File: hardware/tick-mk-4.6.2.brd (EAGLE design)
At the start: 96 x 53 mm, 38 parts, among them IC1 ATMEGA328P, IC2 DS1307, IC3 L7805, Y1 16MHz, Y2 32.768kHz

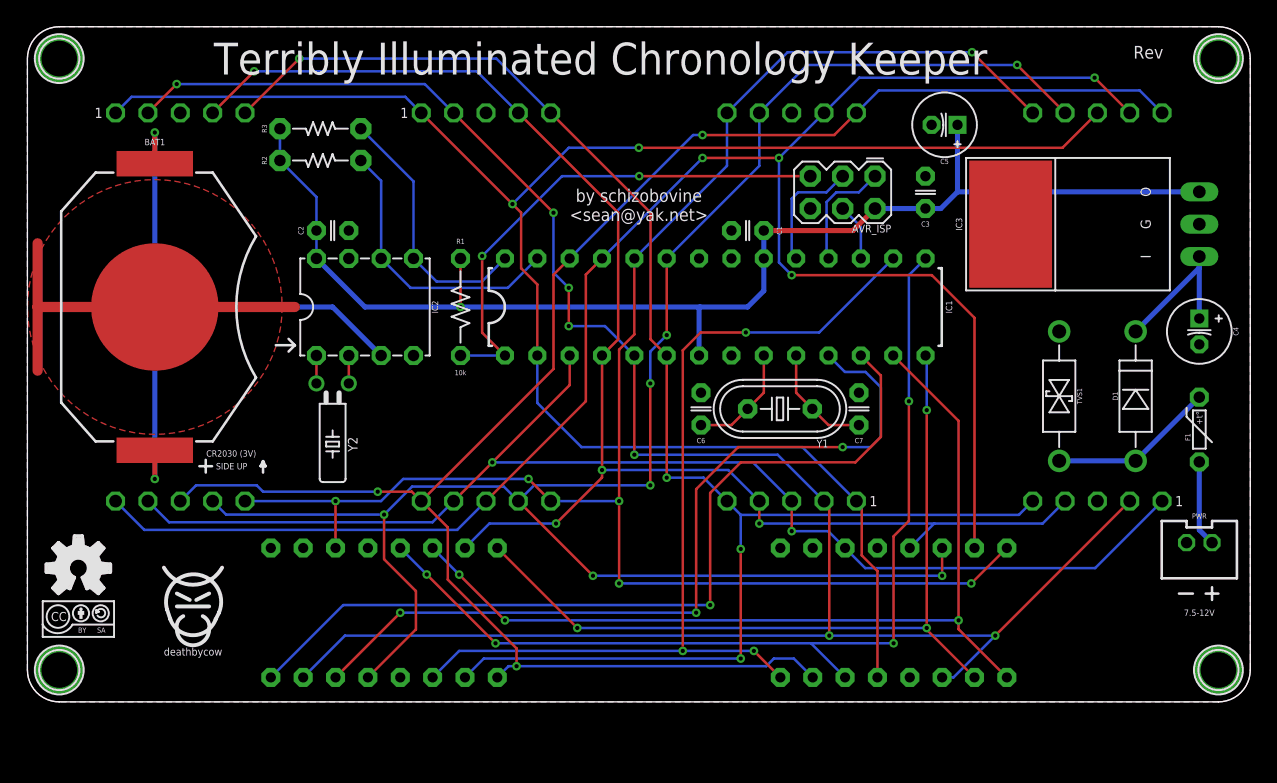
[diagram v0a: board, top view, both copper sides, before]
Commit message: nets complete, now for layout
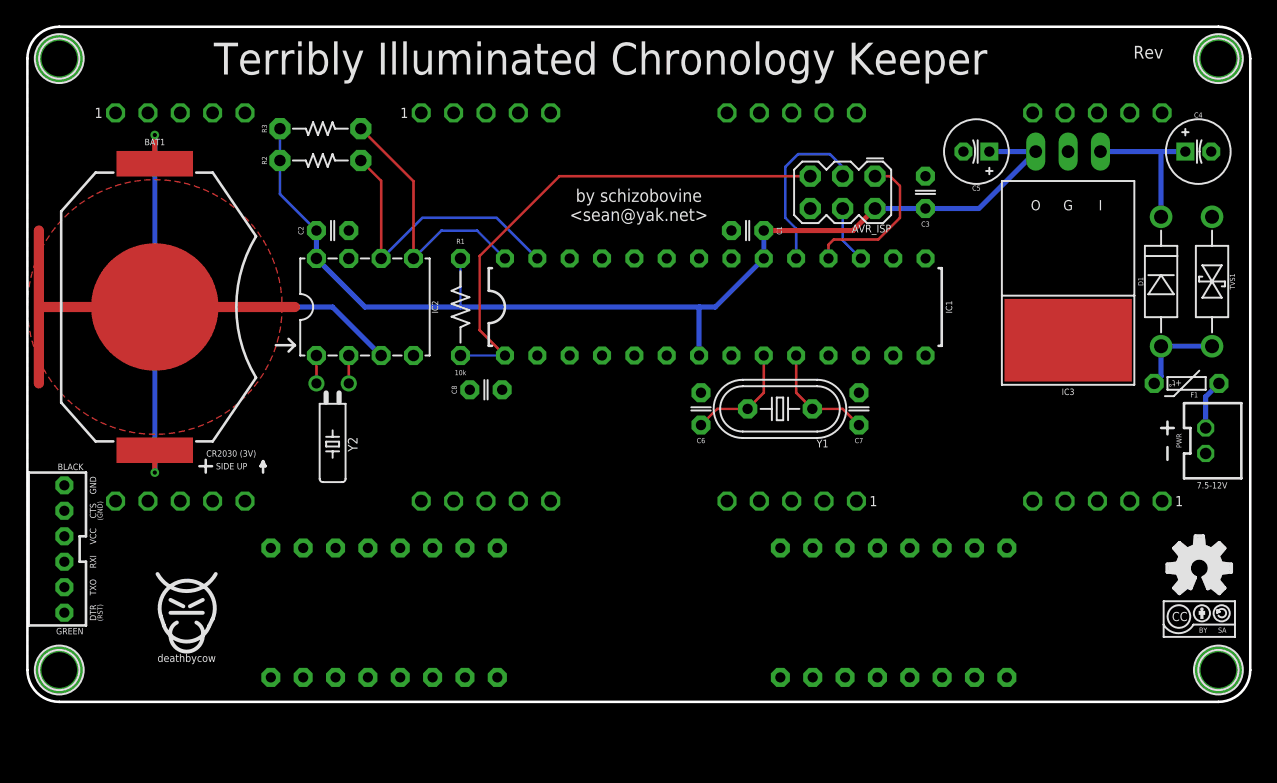
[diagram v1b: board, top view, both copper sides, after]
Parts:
- added C8: 0.1uF, A_butts:C025-024X044
- added JP1: FTDI_CONNJST_PH_VERT_PTH, A_butts:FTDI_CONN_JST_PH_VERT_PTH
- moved U$4 88.0 mm to (92.0, 6.50)
- moved U$5 88.0 mm to (92.0, 10.5)
- moved U$6 88.0 mm to (92.0, 10.5)
- moved U$7 88.0 mm to (92.0, 6.50)
- moved U$3 48.0 mm to (45.0, 19.0)
- moved DISPLAY1 40.0 mm to (68.0, 7.00)
- moved DISPLAY2 40.0 mm to (28.0, 7.00)
- moved TVS1 15.0 mm to (93.0, 33.0)
- moved C4 14.1 mm to (91.9, 43.2), turned to 0 degrees
- moved D1 9.22 mm to (89.0, 33.0)
- moved PWR 8.02 mm to (92.5, 20.5), turned to 270 degrees
- moved IC3 6.76 mm to (81.7, 39.4), turned to 180 degrees
- moved F1 3.76 mm to (91.0, 25.0), turned to 180 degrees
- moved C5 3.26 mm to (74.5, 43.2)
- moved U$2 0.71 mm to (12.5, 7.50)
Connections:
- removed net D0: DIGIT1.8, DIGIT2.1, DIGIT3.1, DIGIT4.1, DISPLAY2.5, IC1.2
- removed net D1: DIGIT1.1, DIGIT2.3, DIGIT3.9, DIGIT4.9, DISPLAY2.11, IC1.3
- new net DTR: C8.1, JP1.DTR
- new net RX: IC1.2, JP1.RXI
- new net TX: IC1.3, JP1.TXO
- net A0: now also DIGIT1.9, DIGIT2.9, DIGIT3.9, DIGIT4.9, DISPLAY1.15, DISPLAY2.11; no longer DIGIT1.7, DIGIT2.7, DIGIT3.7, DIGIT4.7, DISPLAY1.5, DISPLAY2.14
- net A1: now also DIGIT1.10, DIGIT2.10, DIGIT3.10, DIGIT4.10, DISPLAY1.7, DISPLAY2.15; no longer DIGIT1.6, DIGIT2.6, DIGIT3.6, DIGIT4.6, DISPLAY1.11, DISPLAY2.16
- net A2: now also DIGIT1.5, DIGIT2.5, DIGIT3.5, DIGIT4.5, DISPLAY1.14, DISPLAY2.7; no longer DIGIT1.9, DIGIT2.9, DIGIT3.8, DIGIT4.10, DISPLAY2.15
- net A3: no longer DIGIT1.10, DIGIT2.10, DIGIT3.10, DIGIT4.8, DISPLAY1.1, DISPLAY2.7
- net D10: now also DIGIT1.6, DIGIT2.6, DIGIT3.6, DIGIT4.6, DISPLAY2.1; no longer DISPLAY1.3, DISPLAY2.8
- net D11/MOSI: now also DIGIT1.4, DIGIT2.4, DIGIT3.4, DIGIT4.4, DISPLAY2.2
- net D12/MISO: now also DIGIT1.2, DIGIT2.2, DIGIT3.2, DIGIT4.2, DISPLAY2.6
- net D13/SCK: now also DIGIT1.1, DIGIT2.1, DIGIT3.1, DIGIT4.1, DISPLAY1.11, DISPLAY2.8
- net D2: now also DIGIT4.8, DISPLAY1.16, DISPLAY2.14; no longer DIGIT1.4, DIGIT2.4, DIGIT3.4, DIGIT4.4, DISPLAY1.15, DISPLAY2.13
- net D3: now also DIGIT3.8, DISPLAY1.13, DISPLAY2.16; no longer DIGIT1.2, DIGIT2.2, DIGIT3.2, DIGIT4.2, DISPLAY1.7, DISPLAY2.3
- net D4: now also DIGIT2.3, DISPLAY1.3, DISPLAY2.13; no longer DIGIT1.5, DIGIT2.5, DIGIT3.5, DIGIT4.5, DISPLAY1.2
- net D5: now also DIGIT1.3, DISPLAY1.5, DISPLAY2.3; no longer DISPLAY1.6
- net D6: now also DISPLAY1.1, DISPLAY2.5; no longer DISPLAY1.8
- net D7: now also DISPLAY1.2; no longer DISPLAY1.14, DISPLAY2.1
- net D8: now also DISPLAY1.6; no longer DISPLAY1.16, DISPLAY2.2
- net D9: now also DIGIT1.7, DIGIT2.7, DIGIT3.7, DIGIT4.7, DISPLAY1.8; no longer DISPLAY1.13, DISPLAY2.6
- net GND: now also JP1.CTS, JP1.GND
- net RST: now also C8.2
- net VCC: now also JP1.VCC
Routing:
- net D3: track 163.5 -> 0.00 mm, vias 7 -> 0
- net A0: track 149.9 -> 0.00 mm, vias 7 -> 0
- net A2: track 145.6 -> 0.00 mm, vias 4 -> 0
- net D0: track 143.2 -> 0.00 mm, vias 2 -> 0
- net A3: track 138.6 -> 0.00 mm, vias 3 -> 0
- net A1: track 134.5 -> 0.00 mm, vias 6 -> 0
- net D4: track 123.9 -> 0.00 mm, vias 4 -> 0
- net D2: track 114.7 -> 0.00 mm, vias 4 -> 0
- net D1: track 100.2 -> 0.00 mm, vias 2 -> 0
- net D9: track 76.9 -> 0.00 mm, vias 4 -> 0
- net D7: track 72.6 -> 0.00 mm, vias 3 -> 0
- net D10: track 72.1 -> 0.00 mm, vias 3 -> 0
- net D6: track 67.9 -> 0.00 mm, vias 1 -> 0
- net D5: track 65.4 -> 0.00 mm, vias 3 -> 0
- net D8: track 63.2 -> 0.00 mm, vias 3 -> 0
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
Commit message: layout done but still need to add battery monitoring circuit
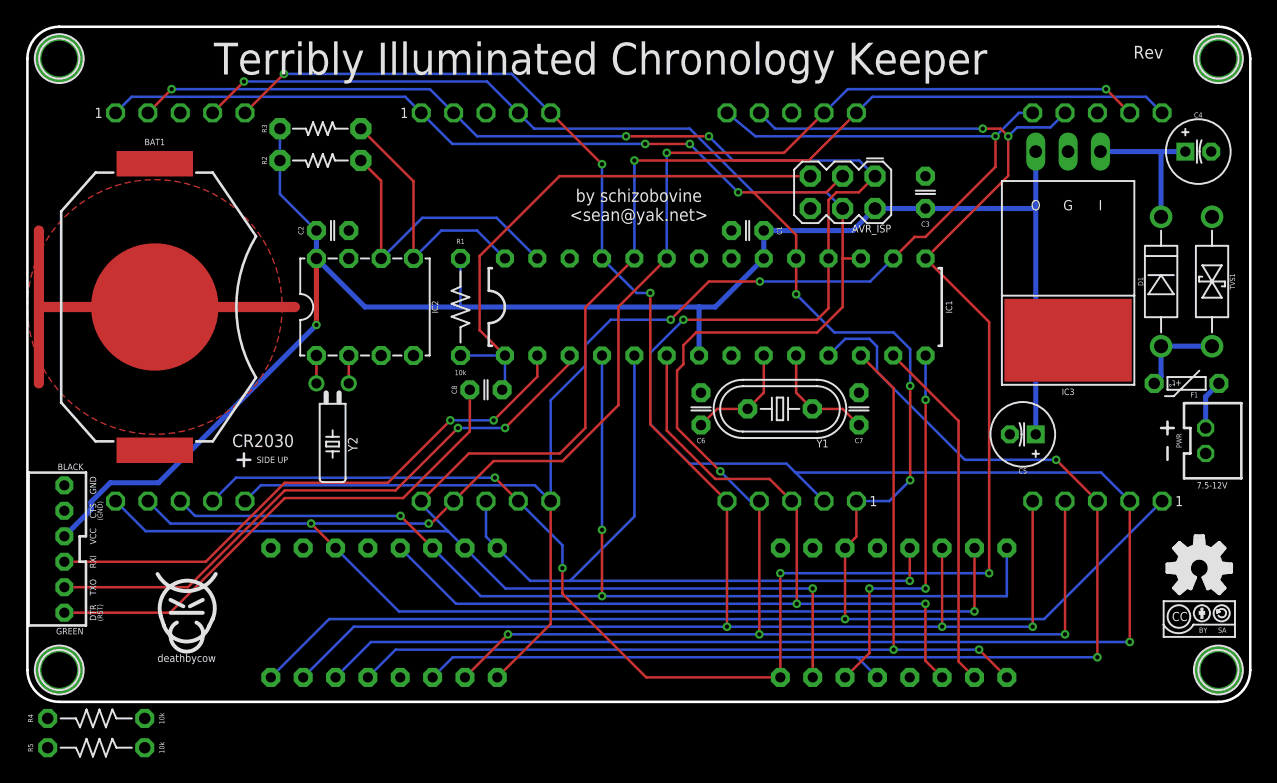
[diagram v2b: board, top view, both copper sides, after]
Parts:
- added R4, R5: 10k, A_butts:RESISTOR-AXIAL-PTH-7.62MM
- moved C5 22.5 mm to (78.1, 21.0)
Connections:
- removed net N$1: BAT1.TOP@1, BAT1.TOP@2, IC2.3
- new net VBAT: BAT1.TOP@1, BAT1.TOP@2, IC2.3, R4.P$1
- net A3: now also R4.P$2, R5.P$1
- net GND: now also R5.P$2
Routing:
- net D12/MISO: track 12.3 -> 212.5 mm, vias 0 -> 5
- net D13/SCK: track 13.6 -> 181.9 mm, vias 0 -> 7
- net A0: track 0.00 -> 162.0 mm, vias 0 -> 5
- net D11/MOSI: track 4.51 -> 162.5 mm, vias 0 -> 5
- net A1: track 0.00 -> 149.7 mm, vias 0 -> 2
- net A2: track 0.00 -> 148.2 mm, vias 0 -> 6
- net D9: track 0.00 -> 143.2 mm, vias 0 -> 6
- net D10: track 0.00 -> 119.8 mm, vias 0 -> 3
- net D5: track 0.00 -> 95.4 mm, vias 0 -> 2
- net D2: track 0.00 -> 90.7 mm, vias 0 -> 3
- net D6: track 0.00 -> 76.1 mm, vias 0 -> 2
- net D4: track 0.00 -> 75.6 mm, vias 0 -> 2
- net D3: track 0.00 -> 59.9 mm, vias 0 -> 1
- net N$1: track 49.8 -> 0.00 mm, vias 2 -> 0
- net VCC: track 87.0 -> 136.0 mm, vias 0 -> 1
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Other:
- board text added: "CR2030"
- board text removed: "CR2030 (3V)"

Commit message: resistor divider to check battery level
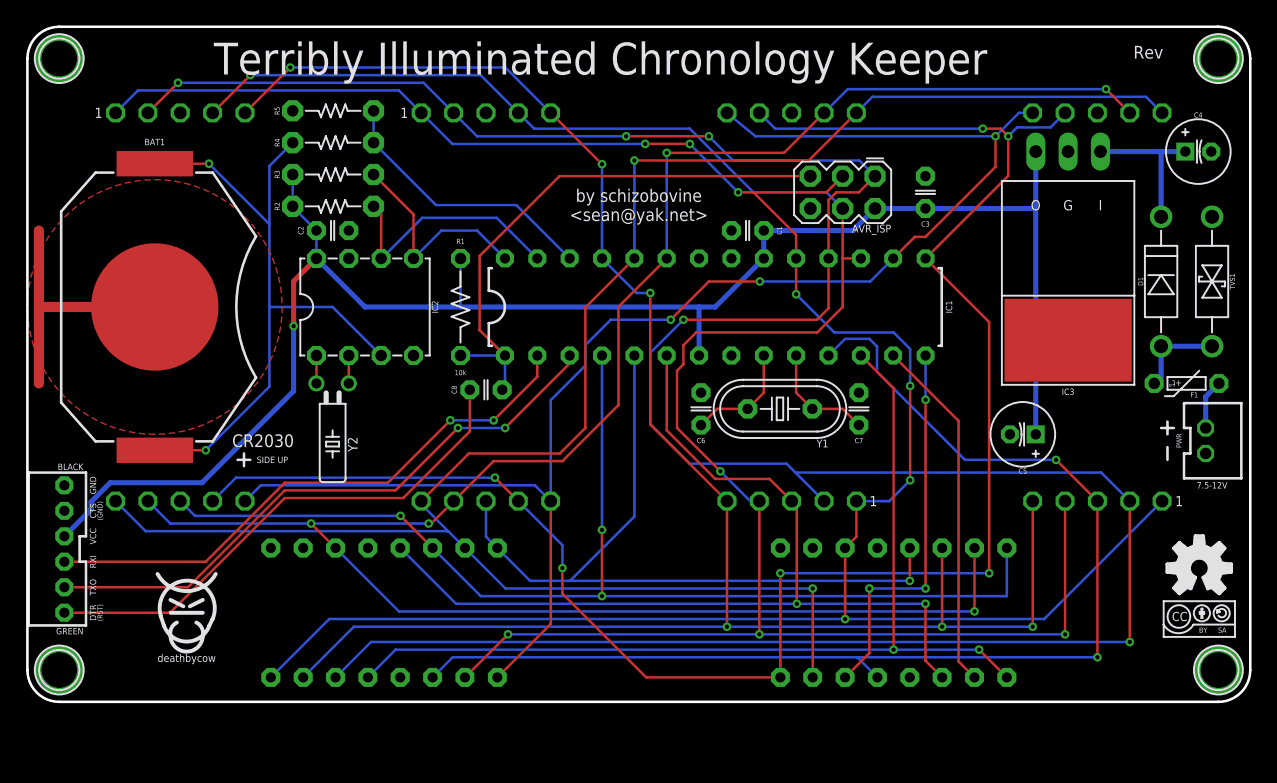
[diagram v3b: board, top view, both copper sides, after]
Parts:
- R4, R5: device A_butts:RESISTOR-AXIAL-PTH-7.62MM -> A_butts:RESISTOR-AXIAL-PTH-6.35MM
- moved R5 53.3 mm to (24.0, 46.4)
- moved R4 48.9 mm to (24.0, 43.9)
- moved R2 3.74 mm to (24.0, 38.9)
- moved R3 3.74 mm to (24.0, 41.4)
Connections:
- net A3: now also R5.P$2; no longer R5.P$1
- net GND: now also R5.P$1; no longer R5.P$2
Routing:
- net VBAT: track 0.00 -> 52.3 mm, vias 0 -> 2
- net A3: track 0.00 -> 21.7 mm
- net GND: track 32.0 -> 21.0 mm
- net SDA: track 23.3 -> 19.2 mm
- net SCL: track 20.9 -> 16.9 mm
- net VCC: track 136.0 -> 134.0 mm

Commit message: finished this layout changed my mind again
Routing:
- net GND: track 21.0 -> 31.2 mm
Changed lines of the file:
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@@
 <vertex x="0" y="50.5" curve="-90"/>
 </polygon>
-<wire x1="1" y1="31" x2="10" y2="31" width="0.8" layer="1"/>
-<wire x1="0.9" y1="25" x2="0.9" y2="37" width="0.8" layer="1"/>
+<wire x1="0.9" y1="31" x2="10" y2="31" width="0.8" layer="1"/>
+<wire x1="0.9" y1="25" x2="0.9" y2="31" width="0.8" layer="1"/>
 <contactref element="JP1" pad="GND"/>
 <contactref element="JP1" pad="CTS"/>
 <contactref element="R5" pad="P$1"/>
-<wire x1="0.9" y1="25" x2="1" y2="31" width="0" layer="19" extent="1-1"/>
+<wire x1="0.9" y1="31" x2="0.9" y2="37" width="0.8" layer="1"/>
+<wire x1="10" y1="31" x2="20.1" y2="31" width="0.8" layer="1"/>
 </signal>
 <signal name="RST">
